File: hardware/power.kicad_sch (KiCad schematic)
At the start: 16 parts, among them Q3 DMG1012T, U2 MAX20049ATED/VY+

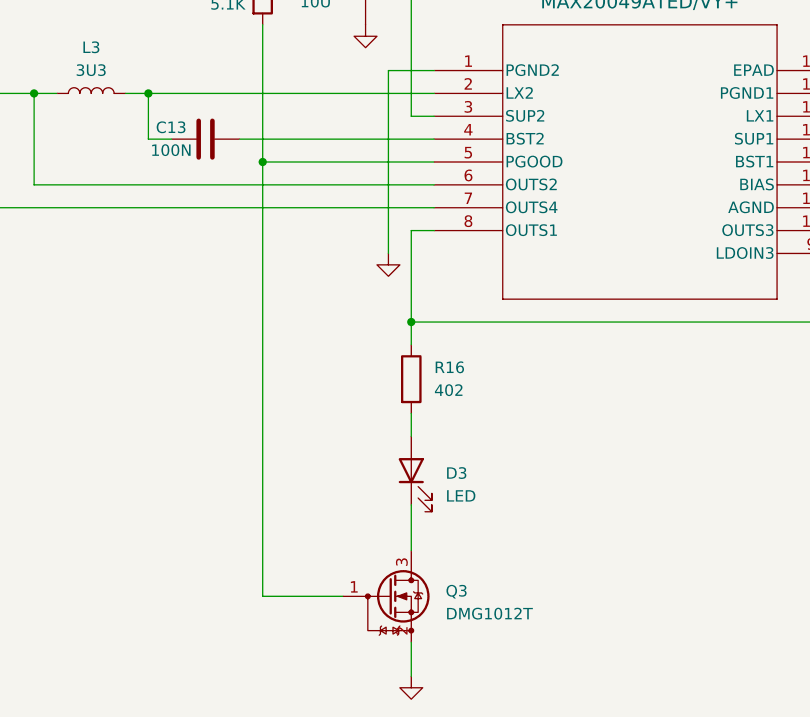
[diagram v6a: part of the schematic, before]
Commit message: cleaned up fakra footprint
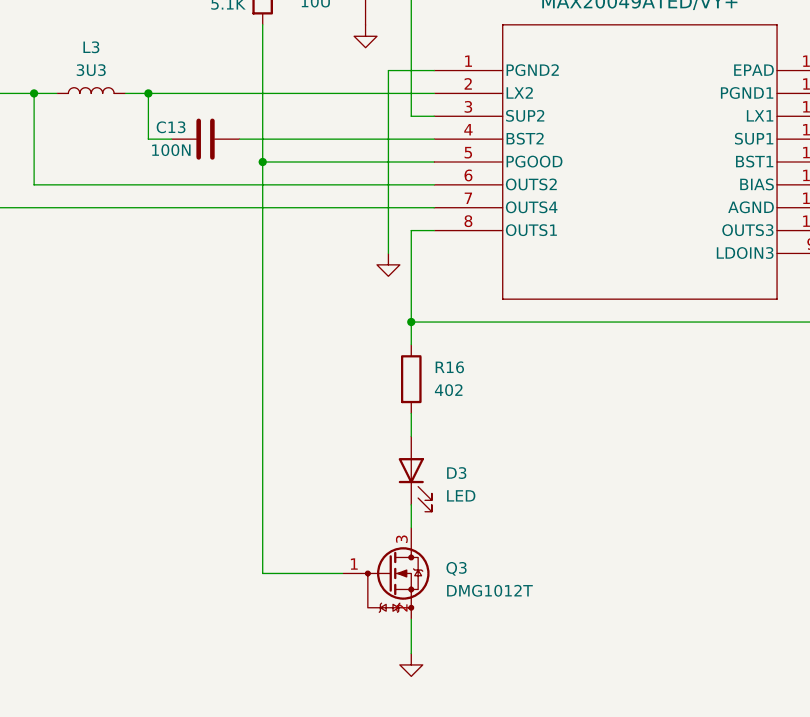
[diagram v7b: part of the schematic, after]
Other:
- moved on the sheet: Q3
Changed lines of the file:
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@@
 	(wire
 		(pts
-			(xy 101.6 144.78) (xy 101.6 148.59)
+			(xy 101.6 142.24) (xy 101.6 146.05)
 		)
 		(stroke
@@
 	(wire
 		(pts
-			(xy 85.09 139.7) (xy 93.98 139.7)
+			(xy 85.09 137.16) (xy 93.98 137.16)
 		)
 		(stroke
@@
 	(wire
 		(pts
-			(xy 85.09 91.44) (xy 85.09 139.7)
+			(xy 85.09 91.44) (xy 85.09 137.16)
 		)
 		(stroke
@@
 	(wire
 		(pts
-			(xy 101.6 129.54) (xy 101.6 134.62)
+			(xy 101.6 129.54) (xy 101.6 132.08)
 		)
 		(stroke
@@
 	(symbol
 		(lib_id "power:GND")
-		(at 101.6 148.59 0)
+		(at 101.6 146.05 0)
 		(unit 1)
 		(exclude_from_sim no)
@@
 		(fields_autoplaced yes)
 		(property "Reference" "#PWR047"
-			(at 101.6 154.94 0)
+			(at 101.6 152.4 0)
 			(effects
 				(font
@@
 		)
 		(property "Value" "GND"
-			(at 101.6 153.67 0)
+			(at 101.6 151.13 0)
 			(effects
 				(font
@@
 		)
 		(property "Footprint" ""
-			(at 101.6 148.59 0)
+			(at 101.6 146.05 0)
 			(effects
 				(font
@@
 		)
 		(property "Datasheet" ""
-			(at 101.6 148.59 0)
+			(at 101.6 146.05 0)
 			(effects
 				(font
@@
 		)
 		(property "Description" "Power symbol creates a global label with name \"GND\" , ground"
-			(at 101.6 148.59 0)
+			(at 101.6 146.05 0)
 			(effects
 				(font
@@
 	(symbol
 		(lib_id "Transistor_FET:DMG1012T")
-		(at 99.06 139.7 0)
+		(at 99.06 137.16 0)
 		(unit 1)
 		(exclude_from_sim no)
@@
 		(fields_autoplaced yes)
 		(property "Reference" "Q3"
+			(at 105.41 136.5884 0)
+			(effects
+				(font
+					(size 1.27 1.27)
+				)
+				(justify left)
+			)
+		)
+		(property "Value" "DMG1012T"
 			(at 105.41 139.1284 0)
 			(effects
@@
 			)
 		)
-		(property "Value" "DMG1012T"
-			(at 105.41 141.6684 0)
+		(property "Footprint" "Package_TO_SOT_SMD:SOT-523"
+			(at 104.14 139.065 0)
 			(effects
 				(font
@@
 				)
 				(justify left)
-			)
-		)
-		(property "Footprint" "Package_TO_SOT_SMD:SOT-523"
-			(at 104.14 141.605 0)
+				(hide yes)
+			)
+		)
+		(property "Datasheet" "https://www.diodes.com/assets/Datasheets/ds31783.pdf"
+			(at 104.14 140.97 0)
 			(effects
 				(font
@@
 			)
 		)
-		(property "Datasheet" "https://www.diodes.com/assets/Datasheets/ds31783.pdf"
-			(at 104.14 143.51 0)
-			(effects
-				(font
-					(size 1.27 1.27)
-				)
-				(justify left)
-				(hide yes)
-			)
-		)
 		(property "Description" "20V Vds, 0.63 Id, N-Channel MOSFET with ESD protection, SOT-523"
-			(at 99.06 139.7 0)
-			(effects
-				(font
+			(at 99.06 137.16 0)
+			(effects
+				(font

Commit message: prepping for fab
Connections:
- net +3V3: now also L4.1; no longer L4.2
- net at C15.2, U2.15 (LX1): now also L4.2; no longer L4.1
